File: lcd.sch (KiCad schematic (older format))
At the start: 1 part, among them J13 CON_1X40

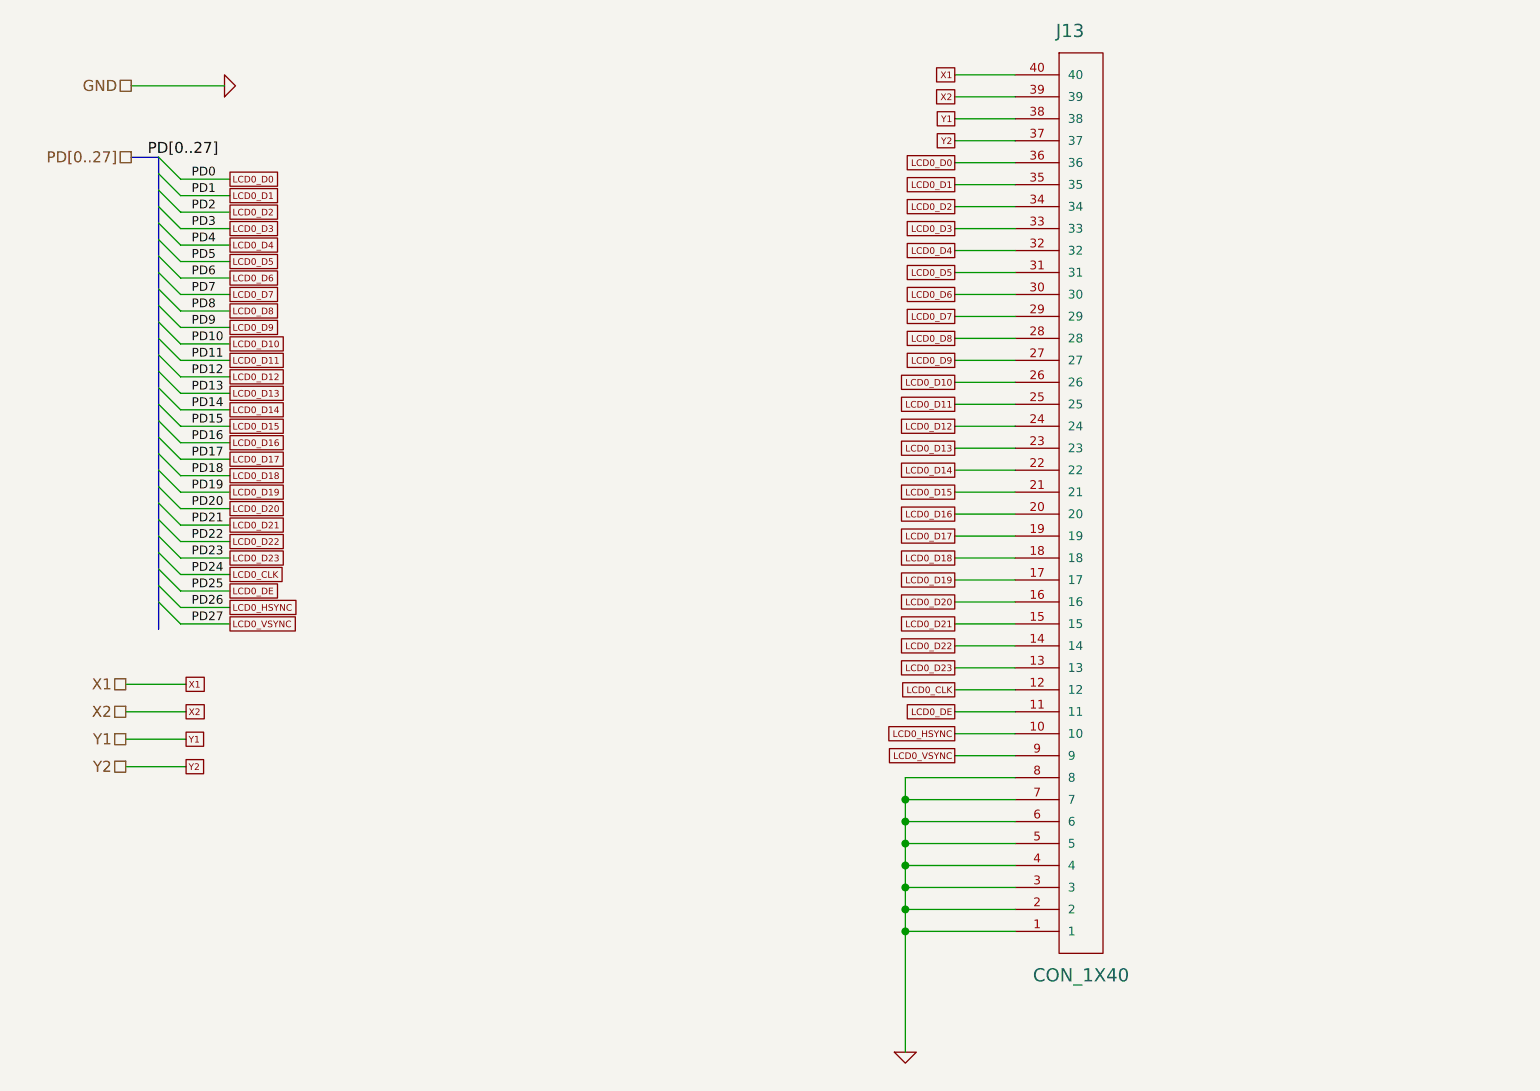
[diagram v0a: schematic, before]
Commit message: 1.4
Fix some issues
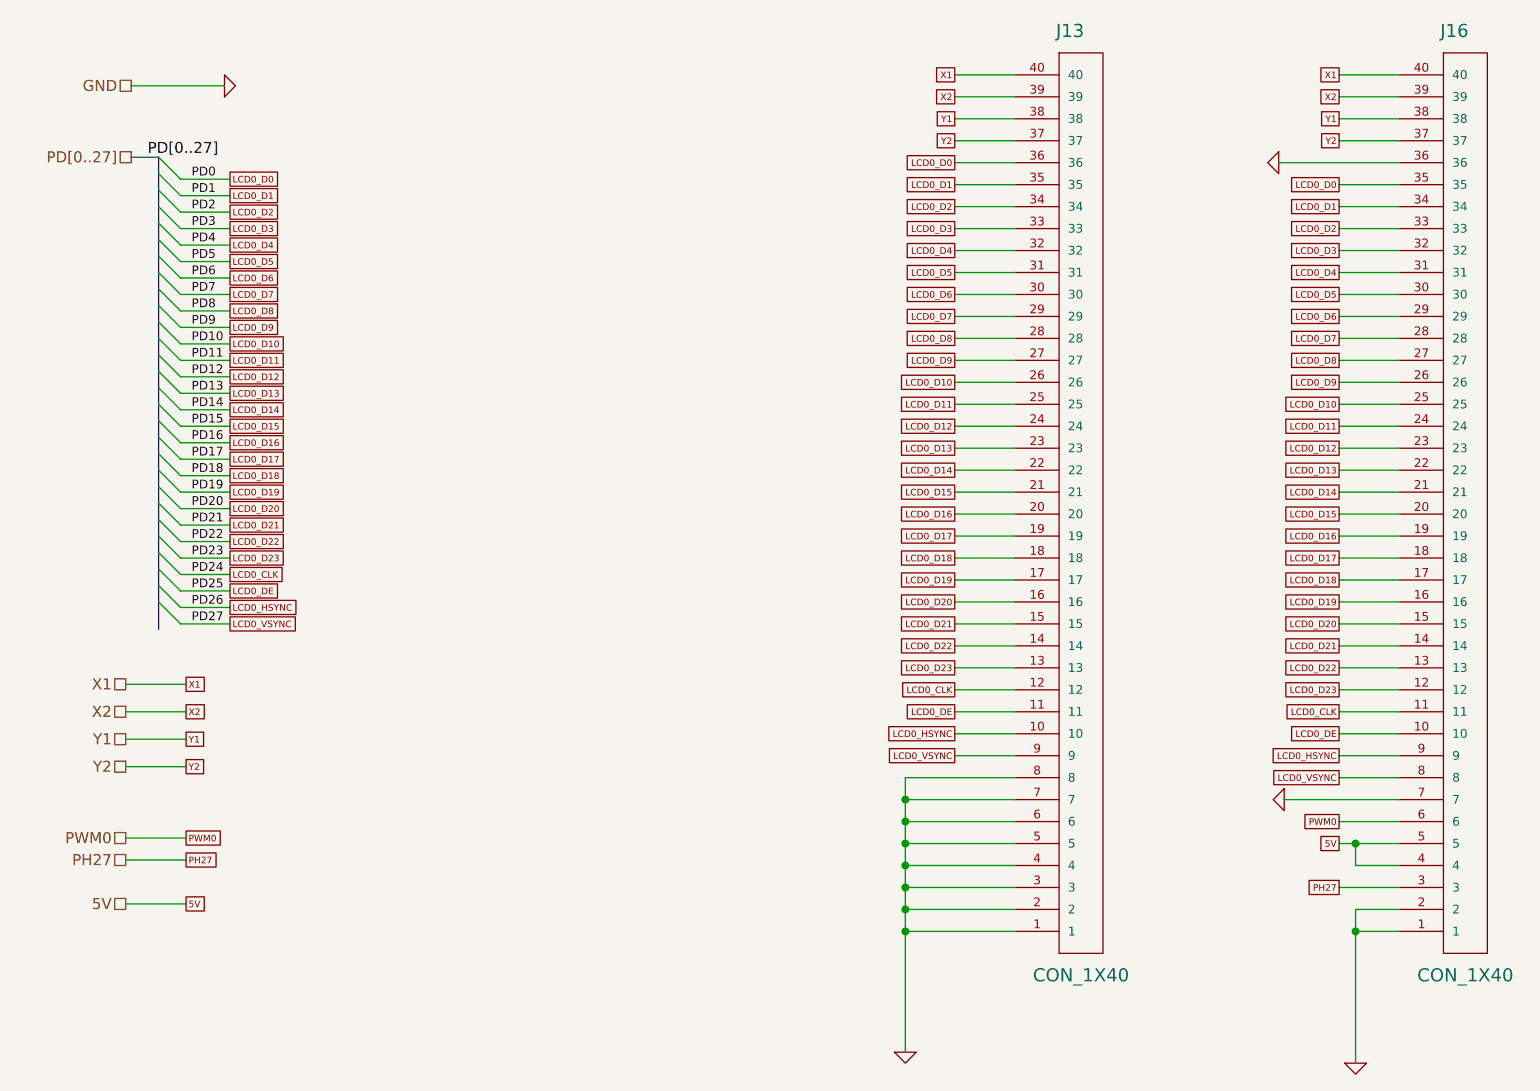
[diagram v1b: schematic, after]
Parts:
- added J16: CON_1X40, symbol CON_1X40
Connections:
- net GND: now also J16.1, J16.2, J16.36, J16.7
- net LCD0_CLK: now also J16.11
- net LCD0_D0: now also J16.35
- net LCD0_D1: now also J16.34
- net LCD0_D10: now also J16.25
- net LCD0_D11: now also J16.24
- net LCD0_D12: now also J16.23
- net LCD0_D13: now also J16.22
- net LCD0_D14: now also J16.21
- net LCD0_D15: now also J16.20
- net LCD0_D16: now also J16.19
- net LCD0_D17: now also J16.18
- net LCD0_D18: now also J16.17
- net LCD0_D19: now also J16.16
- net LCD0_D2: now also J16.33
- net LCD0_D20: now also J16.15
- net LCD0_D21: now also J16.14
- net LCD0_D22: now also J16.13
- net LCD0_D23: now also J16.12
- net LCD0_D3: now also J16.32
- net LCD0_D4: now also J16.31
- net LCD0_D5: now also J16.30
- net LCD0_D6: now also J16.29
- net LCD0_D7: now also J16.28
- net LCD0_D8: now also J16.27
- net LCD0_D9: now also J16.26
- net LCD0_DE: now also J16.10
- net LCD0_HSYNC: now also J16.9
- net LCD0_VSYNC: now also J16.8
- net X1: now also J16.40
- net X2: now also J16.39
- net Y1: now also J16.38
- net Y2: now also J16.37
- new net 5V: J16.4, J16.5
- new net PH27: J16.3
- new net PWM0: J16.6
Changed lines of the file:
@@
 Sheet 11 11
 Title ""
-Date "19 sep 2014"
+Date "25 nov 2014"
 Rev ""
 Comp ""
@@
 GND
 $Comp
-L GND #PWR0197
+L GND #PWR0226
 U 1 1 53E5CB9F
 P 1850 1600
-F 0 "#PWR0197" H 1850 1600 30  0001 C CNN
+F 0 "#PWR0226" H 1850 1600 30  0001 C CNN
 F 1 "GND" H 1850 1530 30  0001 C CNN
 F 2 "" H 1850 1600 60  0000 C CNN
@@
 Y2
 $Comp
-L GND #PWR0198
+L GND #PWR0227
 U 1 1 53E5E13A
 P 4950 6000
-F 0 "#PWR0198" H 4950 6000 30  0001 C CNN
+F 0 "#PWR0227" H 4950 6000 30  0001 C CNN
 F 1 "GND" H 4950 5930 30  0001 C CNN
 F 2 "" H 4950 6000 60  0000 C CNN
@@
 Wire Wire Line
 	5450 1950 5175 1950
+$Comp
+L CON_1X40 J16
+U 1 1 544BA6A1
+P 7200 5450
+F 0 "J16" H 7450 1350 60  0000 C CNN
+F 1 "CON_1X40" H 7500 5650 60  0000 C CNN
+F 2 "" H 7200 5450 60  0000 C CNN
+F 3 "" H 7200 5450 60  0000 C CNN
+	1    7200 5450
+	1    0    0    1
+$EndComp
+Text GLabel 6925 2050 0    30   UnSpc ~ 0
+LCD0_D0
+Text GLabel 6925 2150 0    30   UnSpc ~ 0
+LCD0_D1
+Text GLabel 6925 2250 0    30   UnSpc ~ 0
+LCD0_D2
+Text GLabel 6925 2350 0    30   UnSpc ~ 0
+LCD0_D3
+Text GLabel 6925 2450 0    30   UnSpc ~ 0
+LCD0_D4
+Text GLabel 6925 2550 0    30   UnSpc ~ 0
+LCD0_D5
+Text GLabel 6925 2650 0    30   UnSpc ~ 0
+LCD0_D6
+Text GLabel 6925 2750 0    30   UnSpc ~ 0
+LCD0_D7
+Text GLabel 6925 2850 0    30   UnSpc ~ 0
+LCD0_D8
+Text GLabel 6925 2950 0    30   UnSpc ~ 0
+LCD0_D9
+Text GLabel 6925 3050 0    30   UnSpc ~ 0
+LCD0_D10
+Text GLabel 6925 3150 0    30   UnSpc ~ 0
+LCD0_D11
+Text GLabel 6925 3250 0    30   UnSpc ~ 0
+LCD0_D12
+Text GLabel 6925 3350 0    30   UnSpc ~ 0
+LCD0_D13
+Text GLabel 6925 3450 0    30   UnSpc ~ 0
+LCD0_D14
+Text GLabel 6925 3550 0    30   UnSpc ~ 0
+LCD0_D15
+Text GLabel 6925 3650 0    30   UnSpc ~ 0
+LCD0_D16
+Text GLabel 6925 3750 0    30   UnSpc ~ 0
+LCD0_D17
+Text GLabel 6925 3850 0    30   UnSpc ~ 0
+LCD0_D18
+Text GLabel 6925 3950 0    30   UnSpc ~ 0
+LCD0_D19
+Text GLabel 6925 4050 0    30   UnSpc ~ 0
+LCD0_D20
+Text GLabel 6925 4150 0    30   UnSpc ~ 0
+LCD0_D21
+Text GLabel 6925 4250 0    30   UnSpc ~ 0
+LCD0_D22
+Text GLabel 6925 4350 0    30   UnSpc ~ 0
+LCD0_D23
+Text GLabel 6925 4450 0    30   UnSpc ~ 0
+LCD0_CLK
+Text GLabel 6925 4550 0    30   UnSpc ~ 0
+LCD0_DE
+Text GLabel 6925 4650 0    30   UnSpc ~ 0
+LCD0_HSYNC
+Text GLabel 6925 4750 0    30   UnSpc ~ 0
+LCD0_VSYNC
+Text GLabel 6925 1550 0    30   UnSpc ~ 0
+X1
+Text GLabel 6925 1650 0    30   UnSpc ~ 0
+X2
+Text GLabel 6925 1750 0    30   UnSpc ~ 0
+Y1
+Text GLabel 6925 1850 0    30   UnSpc ~ 0
+Y2
+$Comp
+L GND #PWR0228
+U 1 1 544BA6C7
+P 7000 6050
+F 0 "#PWR0228" H 7000 6050 30  0001 C CNN
+F 1 "GND" H 7000 5980 30  0001 C CNN
+F 2 "" H 7000 6050 60  0000 C CNN
+F 3 "" H 7000 6050 60  0000 C CNN
+	1    7000 6050
+	1    0    0    -1
+$EndComp
+Wire Wire Line
+	7200 1550 6925 1550
+Wire Wire Line
+	7200 1650 6925 1650
+Wire Wire Line
+	7200 1750 6925 1750
+Wire Wire Line
+	7200 1850 6925 1850
+Wire Wire Line
+	6925 4650 7200 4650
+Wire Wire Line
+	7200 4550 6925 4550
+Wire Wire Line
+	7200 4450 6925 4450
+Wire Wire Line
+	7200 4350 6925 4350
+Wire Wire Line
+	7200 4250 6925 4250
+Wire Wire Line
+	7200 4150 6925 4150
+Wire Wire Line
+	7200 4050 6925 4050
+Wire Wire Line
+	7200 3950 6925 3950
+Wire Wire Line
+	7200 3850 6925 3850
+Wire Wire Line
+	7200 3750 6925 3750
+Wire Wire Line
+	7200 3650 6925 3650
+Wire Wire Line
+	7200 3550 6925 3550
+Wire Wire Line
+	7200 3450 6925 3450
+Wire Wire Line
+	7200 3350 6925 3350
+Wire Wire Line
+	7200 3250 6925 3250
+Wire Wire Line
+	7200 3150 6925 3150
+Wire Wire Line
+	7200 3050 6925 3050
+Wire Wire Line
+	7200 2950 6925 2950
+Wire Wire Line
+	7200 2850 6925 2850
+Wire Wire Line
+	7200 2750 6925 2750
+Wire Wire Line
+	7200 2650 6925 2650
+Wire Wire Line
+	7200 2550 6925 2550
+Wire Wire Line
+	7200 2450 6925 2450
+Wire Wire Line
+	7200 2350 6925 2350
+Wire Wire Line
+	7200 2250 6925 2250
+Wire Wire Line
+	7200 2150 6925 2150
+Wire Wire Line
+	7200 2050 6925 2050
+Wire Wire Line
+	6650 1950 7200 1950
+Wire Wire Line
+	7000 6050 7000 5350
+Wire Wire Line
+	7000 5350 7200 5350
+Wire Wire Line
+	7200 5450 7000 5450
+Connection ~ 7000 5450
+Text GLabel 6925 4950 0    30   UnSpc ~ 0
+PWM0
+Text GLabel 6925 5050 0    30   UnSpc ~ 0
+5V
+Wire Wire Line
+	6925 4750 7200 4750
+Wire Wire Line
+	6675 4850 7200 4850
+Wire Wire Line
+	6925 4950 7200 4950
+Wire Wire Line
+	6925 5050 7200 5050
+Text GLabel 1675 5025 2    30   UnSpc ~ 0
+PWM0
+Text HLabel 1400 5025 0    50   UnSpc ~ 0
+PWM0
+Text HLabel 1400 5125 0    50   UnSpc ~ 0
+PH27
+Text GLabel 1675 5125 2    30   UnSpc ~ 0
+PH27
+Text GLabel 1675 5325 2    30   UnSpc ~ 0
+5V
+Text HLabel 1400 5325 0    50   UnSpc ~ 0
+5V
+Wire Wire Line
+	1400 5025 1675 5025
+Wire Wire Line
+	1400 5125 1675 5125
+Wire Wire Line
+	1400 5325 1675 5325
+$Comp
+L GND #PWR0229
+U 1 1 545218F8
+P 6650 1950
+F 0 "#PWR0229" H 6650 1950 30  0001 C CNN
+F 1 "GND" H 6650 1880 30  0001 C CNN
+F 2 "" H 6650 1950 60  0000 C CNN
+F 3 "" H 6650 1950 60  0000 C CNN
+	1    6650 1950
+	0    1    1    0
+$EndComp
+$Comp
+L GND #PWR0230
+U 1 1 54521900
+P 6675 4850
+F 0 "#PWR0230" H 6675 4850 30  0001 C CNN
+F 1 "GND" H 6675 4780 30  0001 C CNN
+F 2 "" H 6675 4850 60  0000 C CNN
+F 3 "" H 6675 4850 60  0000 C CNN
+	1    6675 4850
+	0    1    1    0
+$EndComp
+Wire Wire Line
+	7200 5150 7000 5150
+Wire Wire Line
+	7000 5150 7000 5050
+Connection ~ 7000 5050
+Text GLabel 6925 5250 0    30   UnSpc ~ 0
+PH27
+Wire Wire Line
+	7200 5250 6925 5250
 $EndSCHEMATC
